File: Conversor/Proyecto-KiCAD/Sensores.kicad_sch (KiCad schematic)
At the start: 2 parts

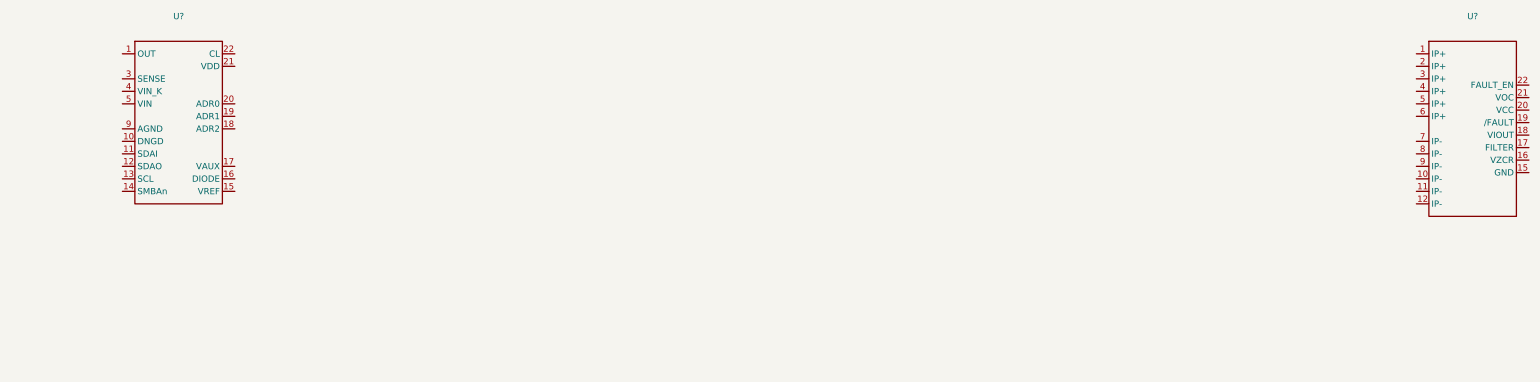
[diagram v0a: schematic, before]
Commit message: Comenzar con la conexion del LM5056A
- Hay que ver el valor de la resistencia shunt RS
- Fijarse si se puede poner los sensores en un archivo distinto
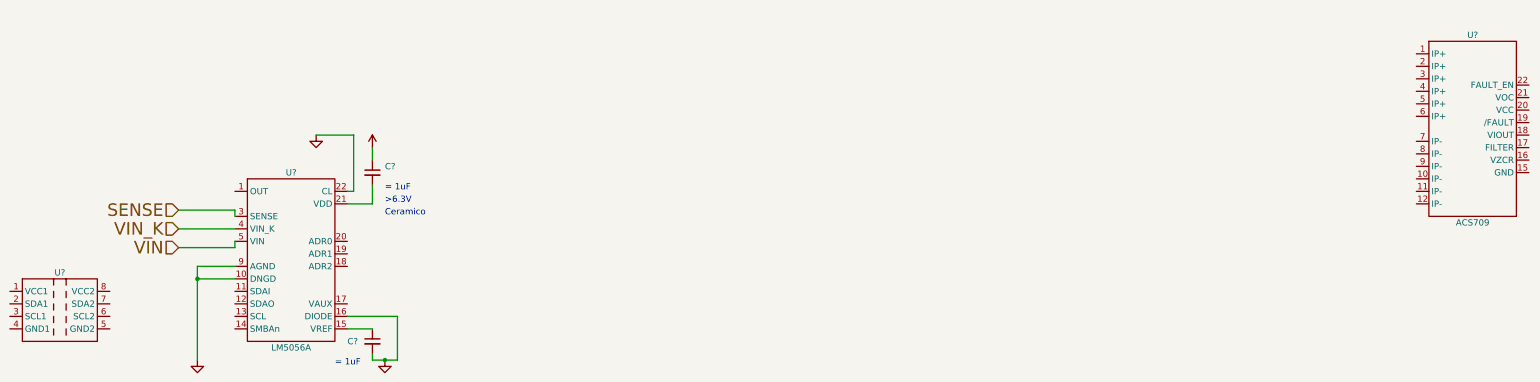
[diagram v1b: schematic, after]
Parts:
- added C? (x2): (no value), symbol Device:C_Small
- added U?: (no value), symbol Componentes proyecto:ISO1640B
- U?: value (none) -> LM5056A
- U?: value (none) -> ACS709
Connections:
- net GND1: now reaches U?.10 (DNGD)
- net GND1: now also U?.16 (DIODE), U?.22 (CL), U?.9 (AGND), C?.2
- net at U?.15 (VREF): now also C?.1
- net at U?.21 (VDD): now also C?.2
- net SENSE: now reaches U?.3 (SENSE)
- net VIN_K: now reaches U?.4 (VIN_K)
- net VIN: now reaches U?.5 (VIN)
- new net +5V: C?.1
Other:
- note added: "= 1uF"
- note added: ">6.3V"
- note added: "Ceramico"
- moved on the sheet: U?
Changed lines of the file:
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@@
 (kicad_sch (version 20211123) (generator eeschema)
   (paper "A3")
-  (symbol (lib_id "Componentes proyecto:LM5056A") (at 115.57 40.64 0) (unit 1)
-    (in_bom yes) (on_board yes) (fields_autoplaced)
-    (property "Reference" "U?" (id 0) (at 115.57 19.05 0))
-    (property "Value" "" (id 1) (at 115.57 21.59 0))
-    (property "Footprint" "" (id 2) (at 115.57 39.37 0)
-      (effects (font (size 1.27 1.27)) hide)
-    )
-    (property "Datasheet" "" (id 3) (at 115.57 39.37 0)
+  (junction (at 119.38 72.39) (diameter 0) (color 0 0 0 0)
+  )
+  (junction (at 157.48 88.9) (diameter 0) (color 0 0 0 0)
+  )
+  (wire (pts (xy 160.02 80.01) (xy 160.02 88.9))
+    (stroke (width 0) (type default) (color 0 0 0 0))
+  )
+  (wire (pts (xy 154.94 82.55) (xy 149.86 82.55))
+    (stroke (width 0) (type default) (color 0 0 0 0))
+  )
+  (wire (pts (xy 151.13 43.18) (xy 151.13 54.61))
+    (stroke (width 0) (type default) (color 0 0 0 0))
+  )
+  (wire (pts (xy 154.94 87.63) (xy 154.94 88.9))
+    (stroke (width 0) (type default) (color 0 0 0 0))
+  )
+  (wire (pts (xy 119.38 69.85) (xy 119.38 72.39))
+    (stroke (width 0) (type default) (color 0 0 0 0))
+  )
+  (wire (pts (xy 154.94 48.26) (xy 154.94 45.72))
+    (stroke (width 0) (type default) (color 0 0 0 0))
+  )
+  (wire (pts (xy 157.48 88.9) (xy 160.02 88.9))
+    (stroke (width 0) (type default) (color 0 0 0 0))
+  )
+  (wire (pts (xy 154.94 88.9) (xy 157.48 88.9))
+    (stroke (width 0) (type default) (color 0 0 0 0))
+  )
+  (wire (pts (xy 154.94 57.15) (xy 154.94 53.34))
+    (stroke (width 0) (type default) (color 0 0 0 0))
+  )
+  (wire (pts (xy 127 69.85) (xy 119.38 69.85))
+    (stroke (width 0) (type default) (color 0 0 0 0))
+  )
+  (wire (pts (xy 127 66.04) (xy 127 64.77))
+    (stroke (width 0) (type default) (color 0 0 0 0))
+  )
+  (wire (pts (xy 151.13 43.18) (xy 143.51 43.18))
+    (stroke (width 0) (type default) (color 0 0 0 0))
+  )
+  (wire (pts (xy 115.57 66.04) (xy 127 66.04))
+    (stroke (width 0) (type default) (color 0 0 0 0))
+  )
+  (wire (pts (xy 149.86 80.01) (xy 160.02 80.01))
+    (stroke (width 0) (type default) (color 0 0 0 0))
+  )
+  (wire (pts (xy 127 58.42) (xy 127 59.69))
+    (stroke (width 0) (type default) (color 0 0 0 0))
+  )
+  (wire (pts (xy 149.86 57.15) (xy 154.94 57.15))
+    (stroke (width 0) (type default) (color 0 0 0 0))
+  )
+  (wire (pts (xy 151.13 54.61) (xy 149.86 54.61))
+    (stroke (width 0) (type default) (color 0 0 0 0))
+  )
+  (wire (pts (xy 119.38 72.39) (xy 127 72.39))
+    (stroke (width 0) (type default) (color 0 0 0 0))
+  )
+  (wire (pts (xy 115.57 62.23) (xy 127 62.23))
+    (stroke (width 0) (type default) (color 0 0 0 0))
+  )
+  (wire (pts (xy 119.38 72.39) (xy 119.38 88.9))
+    (stroke (width 0) (type default) (color 0 0 0 0))
+  )
+  (wire (pts (xy 115.57 58.42) (xy 127 58.42))
+    (stroke (width 0) (type default) (color 0 0 0 0))
+  )
+  (text "= 1uF" (at 147.32 90.17 0)
+    (effects (font (size 1.27 1.27)) (justify left bottom))
+  )
+  (text ">6.3V" (at 157.48 57.15 0)
+    (effects (font (size 1.27 1.27)) (justify left bottom))
+  )
+  (text "Ceramico" (at 157.48 59.69 0)
+    (effects (font (size 1.27 1.27)) (justify left bottom))
+  )
+  (text "= 1uF" (at 157.48 54.61 0)
+    (effects (font (size 1.27 1.27)) (justify left bottom))
+  )
+  (hierarchical_label "SENSE" (shape input) (at 115.57 58.42 180)
+    (effects (font (size 2.54 2.54)) (justify right))
+  )
+  (hierarchical_label "VIN_K" (shape input) (at 115.57 62.23 180)
+    (effects (font (size 2.54 2.54)) (justify right))
+  )
+  (hierarchical_label "VIN" (shape input) (at 115.57 66.04 180)
+    (effects (font (size 2.54 2.54)) (justify right))
+  )
+  (symbol (lib_id "Componentes proyecto:LM5056A") (at 138.43 68.58 0) (unit 1)
+    (in_bom yes) (on_board yes)
+    (property "Reference" "U?" (id 0) (at 138.43 50.8 0))
+    (property "Value" "LM5056A" (id 1) (at 138.43 86.36 0))
+    (property "Footprint" "" (id 2) (at 138.43 67.31 0)
+      (effects (font (size 1.27 1.27)) hide)
+    )
+    (property "Datasheet" "" (id 3) (at 138.43 67.31 0)
       (effects (font (size 1.27 1.27)) hide)
     )
@@
   )
   (symbol (lib_id "Componentes proyecto:ACS709") (at 378.46 41.91 0) (unit 1)
-    (in_bom yes) (on_board yes) (fields_autoplaced)
-    (property "Reference" "U?" (id 0) (at 378.46 19.05 0))
-    (property "Value" "" (id 1) (at 378.46 21.59 0))
+    (in_bom yes) (on_board yes)
+    (property "Reference" "U?" (id 0) (at 378.46 22.86 0))
+    (property "Value" "ACS709" (id 1) (at 378.46 60.96 0))
     (property "Footprint" "" (id 2) (at 378.46 41.91 0)
       (effects (font (size 1.27 1.27)) hide)
@@
     (pin "9")
   )
+  (symbol (lib_id "power:GND1") (at 157.48 88.9 0) (unit 1)
+    (in_bom yes) (on_board yes) (fields_autoplaced)
+    (property "Reference" "#PWR?" (id 0) (at 157.48 95.25 0)
+      (effects (font (size 1.27 1.27)) hide)
+    )
+    (property "Value" "" (id 1) (at 157.48 93.98 0))
+    (property "Footprint" "" (id 2) (at 157.48 88.9 0)
+      (effects (font (size 1.27 1.27)) hide)
+    )
+    (property "Datasheet" "" (id 3) (at 157.48 88.9 0)
+      (effects (font (size 1.27 1.27)) hide)
+    )
+    (pin "1")
+  )
+  (symbol (lib_id "power:GND1") (at 119.38 88.9 0) (unit 1)
+    (in_bom yes) (on_board yes) (fields_autoplaced)
+    (property "Reference" "#PWR?" (id 0) (at 119.38 95.25 0)
+      (effects (font (size 1.27 1.27)) hide)
+    )
+    (property "Value" "" (id 1) (at 119.38 93.98 0))
+    (property "Footprint" "" (id 2) (at 119.38 88.9 0)
+      (effects (font (size 1.27 1.27)) hide)
+    )
+    (property "Datasheet" "" (id 3) (at 119.38 88.9 0)
+      (effects (font (size 1.27 1.27)) hide)
+    )
+    (pin "1")
+  )
+  (symbol (lib_id "Componentes proyecto:ISO1640B") (at 91.44 78.74 0) (unit 1)
+    (in_bom yes) (on_board yes)
+    (property "Reference" "U?" (id 0) (at 91.44 71.12 0))
+    (property "Value" "" (id 1) (at 91.44 86.36 0))
+    (property "Footprint" "" (id 2) (at 91.44 78.74 0)
+      (effects (font (size 1.27 1.27)) hide)
+    )
+    (property "Datasheet" "" (id 3) (at 91.44 78.74 0)
+      (effects (font (size 1.27 1.27)) hide)
+    )
+    (pin "1")
+    (pin "2")
+    (pin "3")
+    (pin "4")
+    (pin "5")
+    (pin "6")
+    (pin "7")
+    (pin "8")
+  )
+  (symbol (lib_id "power:+5V") (at 154.94 45.72 0) (unit 1)
+    (in_bom yes) (on_board yes) (fields_autoplaced)
+    (property "Reference" "#PWR?" (id 0) (at 154.94 49.53 0)
+      (effects (font (size 1.27 1.27)) hide)
+    )
+    (property "Value" "" (id 1) (at 154.94 40.64 0))
+    (property "Footprint" "" (id 2) (at 154.94 45.72 0)
+      (effects (font (size 1.27 1.27)) hide)
+    )
+    (property "Datasheet" "" (id 3) (at 154.94 45.72 0)
+      (effects (font (size 1.27 1.27)) hide)
+    )
+    (pin "1")
+  )
+  (symbol (lib_id "power:GND1") (at 143.51 43.18 0) (unit 1)
+    (in_bom yes) (on_board yes) (fields_autoplaced)
+    (property "Reference" "#PWR?" (id 0) (at 143.51 49.53 0)
+      (effects (font (size 1.27 1.27)) hide)
+    )
+    (property "Value" "" (id 1) (at 143.51 48.26 0))
+    (property "Footprint" "" (id 2) (at 143.51 43.18 0)
+      (effects (font (size 1.27 1.27)) hide)
+    )
+    (property "Datasheet" "" (id 3) (at 143.51 43.18 0)
+      (effects (font (size 1.27 1.27)) hide)
+    )
+    (pin "1")
+  )
+  (symbol (lib_id "Device:C_Small") (at 154.94 85.09 0) (unit 1)
+    (in_bom yes) (on_board yes)
+    (property "Reference" "C?" (id 0) (at 149.86 85.09 0)
+      (effects (font (size 1.27 1.27)) (justify left))
+    )
+    (property "Value" "" (id 1) (at 148.59 87.63 0)
+      (effects (font (size 1.27 1.27)) (justify left))
+    )
+    (property "Footprint" "" (id 2) (at 154.94 85.09 0)
+      (effects (font (size 1.27 1.27)) hide)
+    )
+    (property "Datasheet" "~" (id 3) (at 154.94 85.09 0)
+      (effects (font (size 1.27 1.27)) hide)
+    )
+    (pin "1")
+    (pin "2")
+  )
+  (symbol (lib_id "Device:C_Small") (at 154.94 50.8 0) (unit 1)
+    (in_bom yes) (on_board yes) (fields_autoplaced)
+    (property "Reference" "C?" (id 0) (at 157.48 49.5362 0)
+      (effects (font (size 1.27 1.27)) (justify left))
+    )
+    (property "Value" "" (id 1) (at 157.48 52.0762 0)
+      (effects (font (size 1.27 1.27)) (justify left))
+    )
+    (property "Footprint" "" (id 2) (at 154.94 50.8 0)
+      (effects (font (size 1.27 1.27)) hide)
+    )
+    (property "Datasheet" "~" (id 3) (at 154.94 50.8 0)
+      (effects (font (size 1.27 1.27)) hide)
+    )
+    (pin "1")
+    (pin "2")
+  )
 )

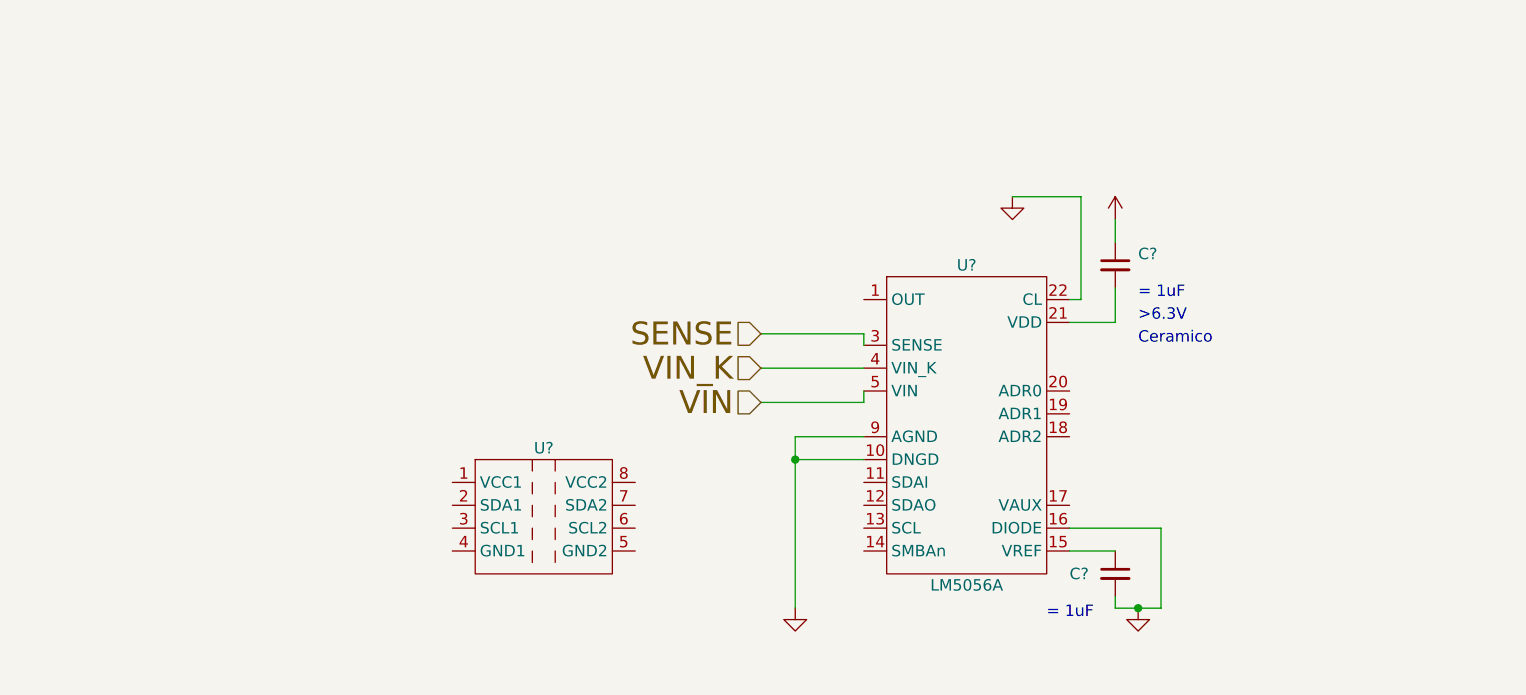
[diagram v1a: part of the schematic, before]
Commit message: Continuar la conexion del esuqematico de sensores
- Agregado y leido un tutorial de I2C de TI
- Pasar de conexiones a la sheet auxiliar -> Global labels
- Aregada la datasheet del DSP que faltaba
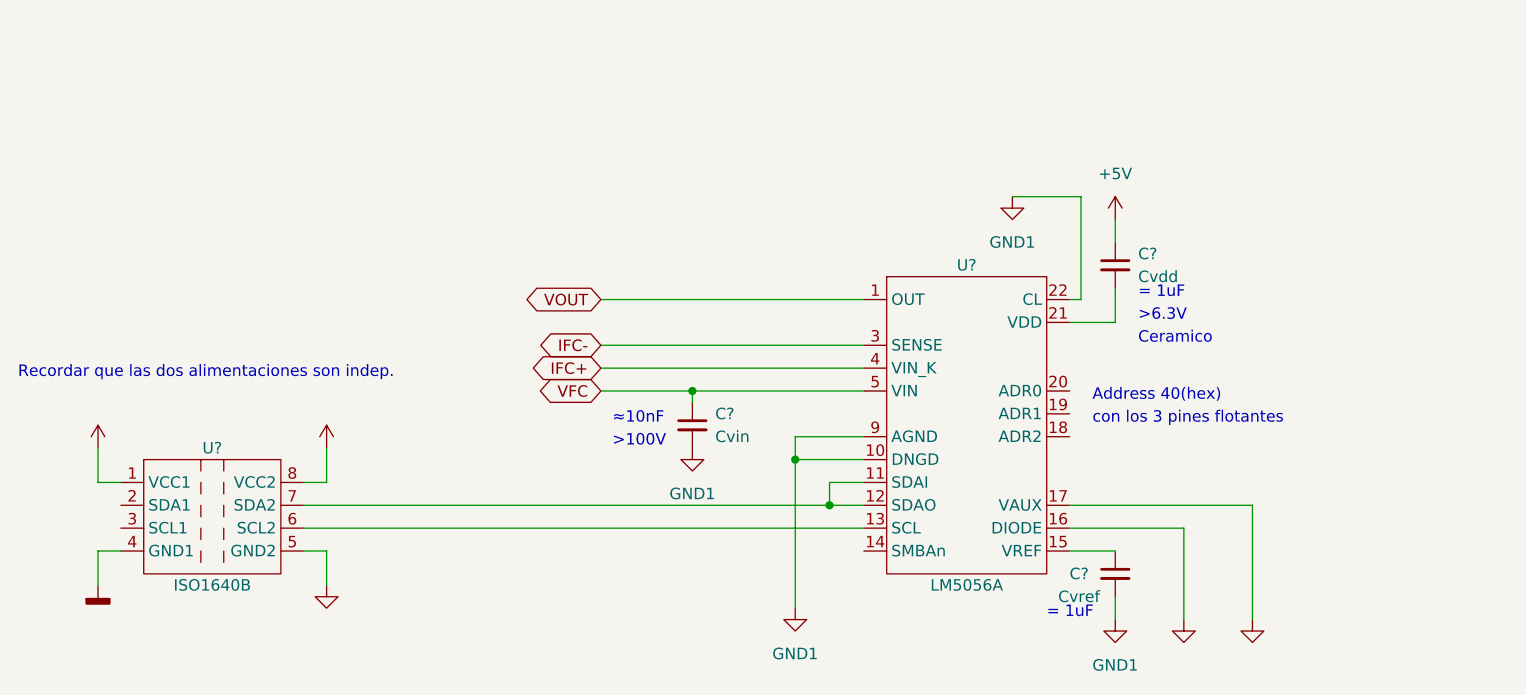
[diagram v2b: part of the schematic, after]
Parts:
- added C?: Cvin, symbol Device:C_Small
- C?: value (none) -> Cvref
- C?: value (none) -> Cvdd
- U?: value (none) -> ISO1640B
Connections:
- net +5V: now also U?.1 (VCC1), U?.8 (VCC2)
- net GND1: now also U?.17 (VAUX), U?.5 (GND2), C?.2
- net VOUT: now reaches U?.1 (OUT)
- net at U?.11 (SDAI): now also U?.12 (SDAO), U?.7 (SDA2)
- net at U?.13 (SCL): now also U?.6 (SCL2)
- net GNDD: now reaches U?.4 (GND1)
- net SENSE renamed IFC-
- net VIN renamed VFC
- net VFC: now also C?.1
- net VIN_K renamed IFC+
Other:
- note added: ">100V"
- note added: "Address 40(hex)"
- note added: "Recordar que las dos alimentaciones son indep."
- note added: "con los 3 pines flotantes"
- note added: "≈10nF"
- moved on the sheet: U?
